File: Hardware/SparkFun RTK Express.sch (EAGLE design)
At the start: 103 parts, among them J13 Internal, J16 microSD, J17 Qwiic Right Angle, J20 FPC_12_0.5MM_BACKFLIP, J3 USB Female Type C Connector, J4 External, J5 USB Female Type C Connector, Q1 SIL2308-TP, Q2 MBT3904DW1T1, U1 74HC4052D, U10 MCP73833, U13 LIS2DH12, U2 AP2112K-3.3, U3 U-BLOX_ZED-F9P, U4 STLQ015-3.3V, U5 ESP-WROOM-3232D-NARROW, U6 CH340C, U7 MAX17048

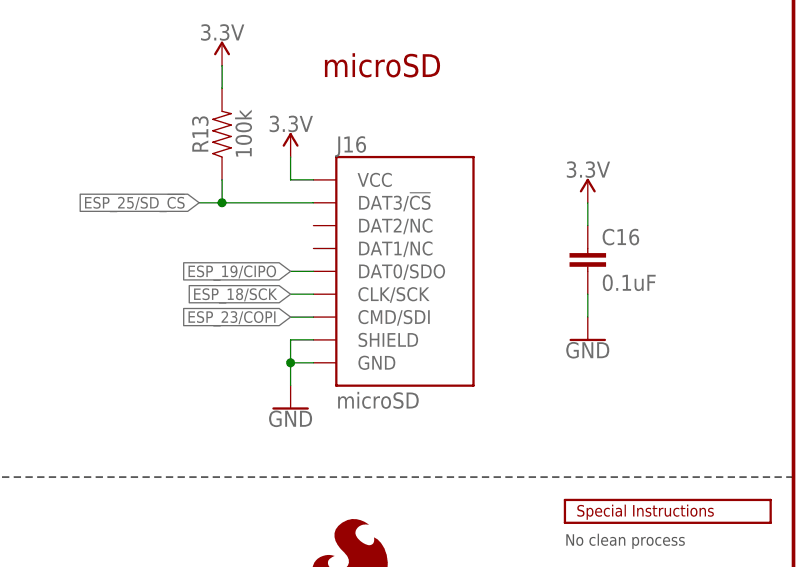
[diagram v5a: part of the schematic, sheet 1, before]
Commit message: Move microSD socket further out.
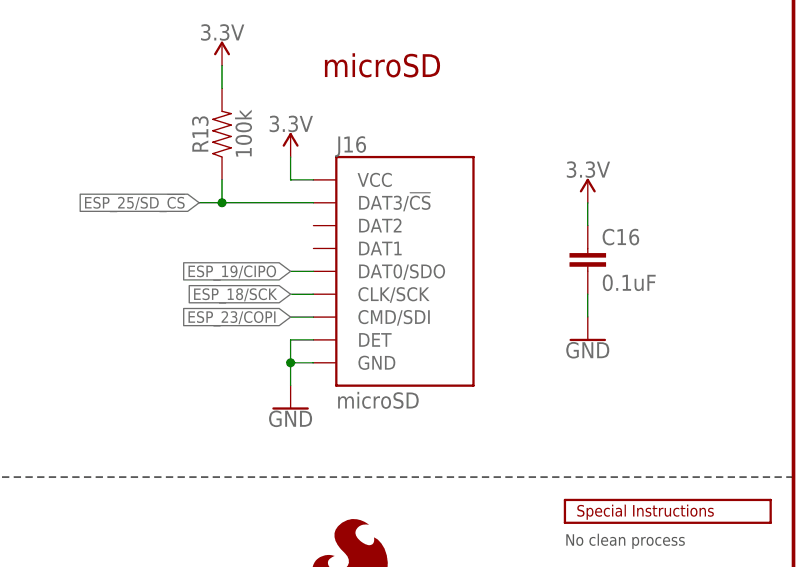
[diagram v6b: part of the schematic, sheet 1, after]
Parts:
- E1: device SparkFun-RF:ANTENNA-SMA-GROUNDEDEDGE_SMA_SMD -> SparkFun-RF:ANTENNA-SMA-GROUNDEDEDGE_SMA
- FB1: device SparkFun-Coils:FERRITE_BEAD-0402-2.66OHM-1GHZ -> SparkFun-Coils:FERRITE_BEAD-0402-2.66Ω-1GHZ
- J16: device SparkFun-Connectors:MICRO-SD-SDIOPUSH-PUSH -> SparkFun-Connectors:MICRO-SDFRICTION
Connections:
- net GND: now also J16.DET; no longer J16.SHIELD
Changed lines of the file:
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@@
 <layer number="56" name="wert" color="7" fill="1" visible="no" active="no"/>
 <layer number="57" name="tCAD" color="7" fill="1" visible="no" active="no"/>
+<layer number="58" name="bCAD" color="7" fill="1" visible="no" active="no"/>
 <layer number="59" name="tCarbon" color="7" fill="1" visible="no" active="no"/>
 <layer number="60" name="bCarbon" color="7" fill="1" visible="no" active="no"/>
@@
 <layer number="250" name="Descript" color="3" fill="1" visible="no" active="no"/>
 <layer number="251" name="SMDround" color="12" fill="11" visible="no" active="no"/>
+<layer number="253" name="Extra" color="7" fill="1" visible="no" active="no"/>
 <layer number="254" name="cooling" color="7" fill="1" visible="yes" active="yes"/>
 <layer number="255" name="routoute" color="7" fill="1" visible="yes" active="yes"/>
@@
 <part name="SUPPLY6" library="SparkFun-PowerSymbols" deviceset="3.3V" device=""/>
 <part name="GND19" library="SparkFun-PowerSymbols" deviceset="GND" device=""/>
-<part name="FB1" library="SparkFun-Coils" deviceset="FERRITE_BEAD" device="-0402-2.66OHM-1GHZ" value="2.66Ω"/>
+<part name="FB1" library="SparkFun-Coils" deviceset="FERRITE_BEAD" device="-0402-2.66Ω-1GHZ" value="2.66Ω"/>
 <part name="LOGO2" library="SparkFun-Aesthetics" deviceset="SFE_LOGO_NAME_FLAME" device=".1_INCH"/>
 <part name="U3" library="SparkFun-GPS" deviceset="U-BLOX_ZED-F9P" device=""/>
@@
 <part name="GND24" library="SparkFun-PowerSymbols" deviceset="GND" device=""/>
 <part name="D6" library="SparkFun-IC-Power" deviceset="PRTR5V0U2" device="F"/>
-<part name="E1" library="SparkFun-RF" deviceset="ANTENNA-SMA-GROUNDED" device="EDGE_SMA_SMD" value="SMA"/>
+<part name="E1" library="SparkFun-RF" deviceset="ANTENNA-SMA-GROUNDED" device="EDGE_SMA" value="SMA"/>
 <part name="FRAME2" library="SparkFun-Aesthetics" deviceset="FRAME-LEDGER" device=""/>
 <part name="GND1" library="SparkFun-PowerSymbols" deviceset="GND" device=""/>
@@
 <part name="SUPPLY28" library="SparkFun-PowerSymbols" deviceset="3.3V" device=""/>
 <part name="D9" library="SparkFun-DiscreteSemi" deviceset="DIODE-SCHOTTKY" device="-BAT60A" value="3A/10V/280mV"/>
-<part name="J16" library="SparkFun-Connectors" deviceset="MICRO-SD-SDIO" device="PUSH-PUSH" value="microSD"/>
+<part name="J16" library="SparkFun-Connectors" deviceset="MICRO-SD" device="FRICTION" value="microSD"/>
 <part name="MEAS" library="SparkFun-Jumpers" deviceset="JUMPER-COMBO_2_NC_TRACE" device="" value=""/>
 <part name="J14" library="SparkFun-Connectors" deviceset="CONN_02" device="1X02_NO_SILK"/>
@@
 <attribute name="VALUE" x="268.478" y="167.386" size="1.778" layer="96" font="vector" rot="MR180" align="top-left"/>
 </instance>
-<instance part="J16" gate="G$1" x="386.08" y="86.36" smashed="yes">
+<instance part="J16" gate="J1" x="386.08" y="86.36" smashed="yes">
 <attribute name="NAME" x="381" y="99.568" size="1.778" layer="95"/>
 <attribute name="VALUE" x="381" y="71.12" size="1.778" layer="96"/>
@@
 <wire x1="375.92" y1="96.52" x2="375.92" y2="99.06" width="0.1524" layer="91"/>
 <pinref part="SUPPLY26" gate="G$1" pin="3.3V"/>
-<pinref part="J16" gate="G$1" pin="VCC"/>
+<pinref part="J16" gate="J1" pin="VCC"/>
 </segment>
 <segment>
@@
 <wire x1="378.46" y1="76.2" x2="375.92" y2="76.2" width="0.1524" layer="91"/>
 <junction x="375.92" y="76.2"/>
-<pinref part="J16" gate="G$1" pin="GND"/>
-<pinref part="J16" gate="G$1" pin="SHIELD"/>
+<pinref part="J16" gate="J1" pin="GND"/>
+<pinref part="J16" gate="J1" pin="DET"/>
 </segment>
 <segment>
@@
 <wire x1="368.3" y1="96.52" x2="368.3" y2="93.98" width="0.1524" layer="91"/>
 <junction x="368.3" y="93.98"/>
-<pinref part="J16" gate="G$1" pin="DAT3/!CS!"/>
+<pinref part="J16" gate="J1" pin="DAT3/!CS!"/>
 </segment>
 </net>
@@
 <wire x1="378.46" y1="83.82" x2="375.92" y2="83.82" width="0.1524" layer="91"/>
 <label x="375.92" y="83.82" size="1.27" layer="95" rot="R180" xref="yes"/>
-<pinref part="J16" gate="G$1" pin="CLK/SCK"/>
+<pinref part="J16" gate="J1" pin="CLK/SCK"/>
 </segment>
 </net>
@@
 <wire x1="378.46" y1="86.36" x2="375.92" y2="86.36" width="0.1524" layer="91"/>
 <label x="375.92" y="86.36" size="1.27" layer="95" rot="R180" xref="yes"/>
-<pinref part="J16" gate="G$1" pin="DAT0/SDO"/>
+<pinref part="J16" gate="J1" pin="DAT0/SDO"/>
 </segment>
 </net>
@@
 <wire x1="378.46" y1="81.28" x2="375.92" y2="81.28" width="0.1524" layer="91"/>
 <label x="375.92" y="81.28" size="1.27" layer="95" rot="R180" xref="yes"/>
-<pinref part="J16" gate="G$1" pin="CMD/SDI"/>
-</segment>
-</net>
+<pinref part="J16" gate="J1" pin="CMD/SDI"/>
+</segment>
+</net>

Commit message: Remove push pull SD socket. v13 PCB
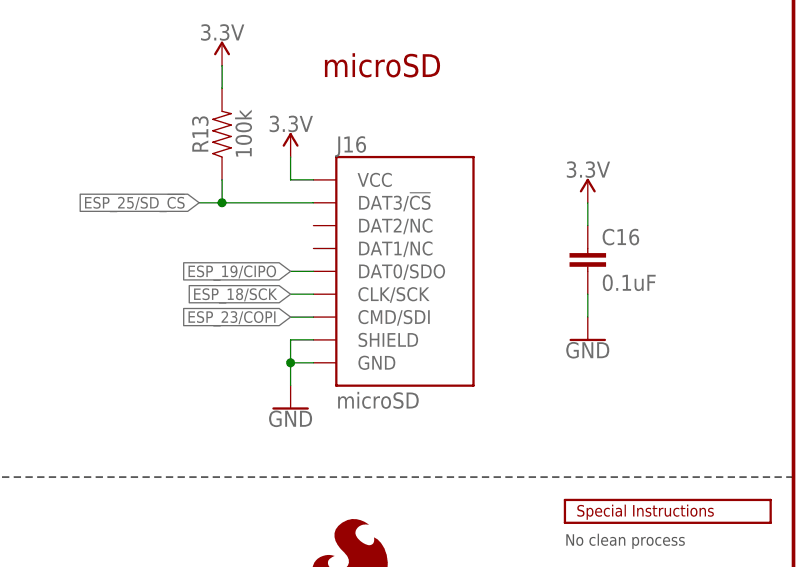
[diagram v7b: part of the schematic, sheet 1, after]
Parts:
- FB1: device SparkFun-Coils:FERRITE_BEAD-0402-2.66Ω-1GHZ -> SparkFun-Coils:FERRITE_BEAD-0402-2.66OHM-1GHZ
- J16: device SparkFun-Connectors:MICRO-SDFRICTION -> SparkFun-Connectors:MICRO-SD-SDIOPUSH-PUSH
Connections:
- net GND: now also J16.SHIELD; no longer J16.DET

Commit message: Remove groundplane from around accel. Switch to wider ESP FP, exposed pin microSD, CH340 with VCC from USB.
Increase paste on 12-pin FPC connector.
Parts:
- removed J16: microSD, SparkFun-Connectors:MICRO-SD-SDIOPUSH-PUSH
- added J19: MICRO-SD-PUSH-PUSH-EXT-PIN, SparkFun-Connectors:MICRO-SD-PUSH-PUSH-EXT-PIN
- added R33: 3.3k, SparkFun-Resistors:3.3KOHM-0603-1/10W-1%
- added R34: 10k, SparkFun-Resistors:10KOHM-0603-1/10W-1%
- D10: value PESD0402 -> PESD0402-0402; device SparkFun-DiscreteSemi:PESD0402 -> SparkFun-DiscreteSemi:PESD0402-0402
- FB1: device SparkFun-Coils:FERRITE_BEAD-0402-2.66OHM-1GHZ -> SparkFun-Coils:FERRITE_BEAD-0402-2.66Ω-1GHZ
- J20: value FPC_12_0.5MM_BACKFLIP -> (none); device RTK Facet:FPC_12_0.5MM_BACKFLIP -> SparkFun-Connectors:CONN_12FPC_12_0.5MM
- U5: value ESP-WROOM-3232D-NARROW -> ESP-WROOM-3232D; device SparkFun-RF:ESP-WROOM-3232D-NARROW -> SparkFun-RF:ESP-WROOM-3232D
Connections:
- removed net ESP_I35: U5.IA35
- new net ESP_I35/DEVICE_SENSE: R33.2, R34.1, U5.IA35
- new net N$1: C13.1, C14.1, U6.V3
- net 3.3V: now also J19.VCC, R34.2; no longer C13.1, C14.1, J16.VCC, U6.V3, U6.VCC
- net ESP_18/SCK: now also J19.CLK/SCK; no longer J16.CLK/SCK
- net ESP_19/CIPO: now also J19.DAT0/SDO; no longer J16.DAT0/SDO
- net ESP_23/COPI: now also J19.CMD/SDI; no longer J16.CMD/SDI
- net ESP_25/SD_!CS!: now also J19.DAT3/!CS!; no longer J16.DAT3/!CS!
- net GND: now also J19.DET, J19.GND, R33.1; no longer J16.GND, J16.SHIELD
- net V_USB: now also U6.VCC
